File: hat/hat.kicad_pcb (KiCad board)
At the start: 4 copper layers, 45 parts, among them IC1 LM2676S-5.0, IC2 DMMT5401-7-F, J1 Conn_Coaxial, J2 nfc, J3 52840 tx pri rx, J4 52840 rx rpi tx, J5 Conn_ARM_JTAG_SWD_10, J6 Raspberry_Pi_2_3, J7 Screw_Terminal_01x02, J8 Screw_Terminal_01x01, P1 Conn_02x08_Odd_Even, P2 Conn_02x20_Odd_Even, Q1 DMG2305UX-7, U1 nRF52840-QIAA, Y1 32mhzCrystal

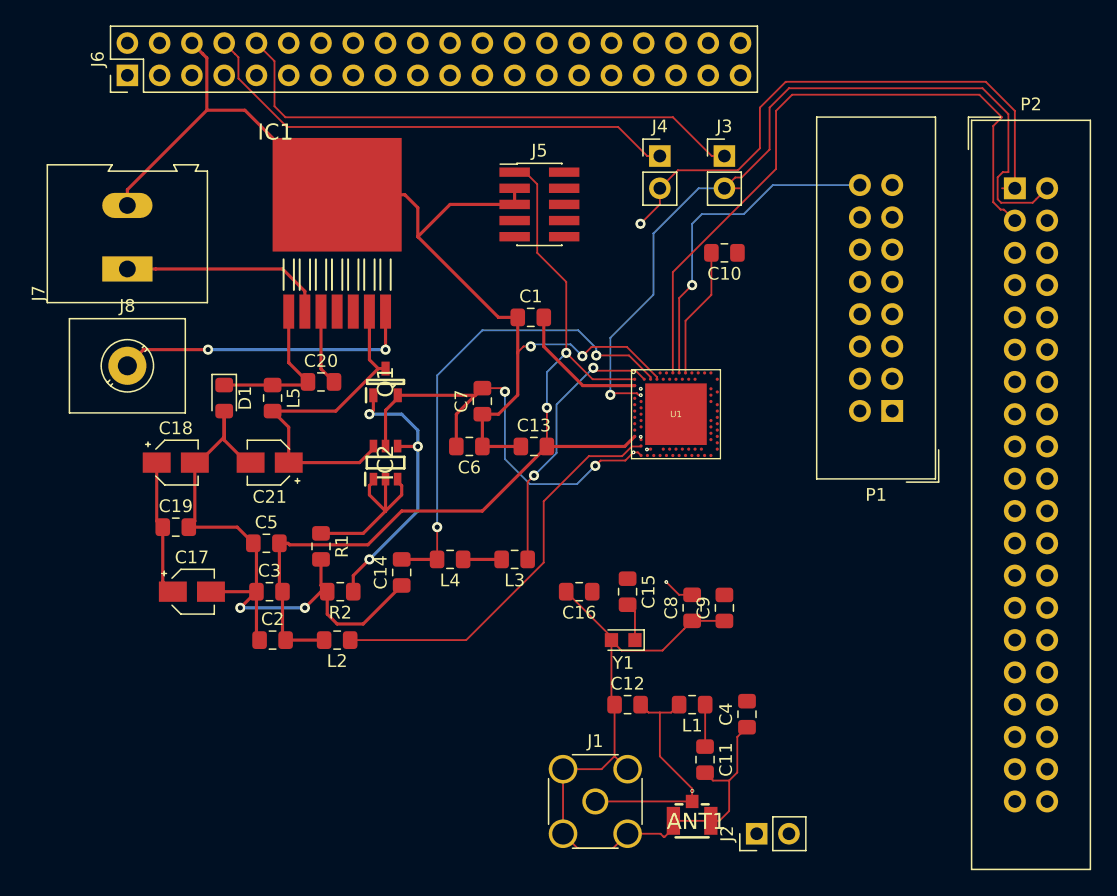
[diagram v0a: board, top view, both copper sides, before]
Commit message: made more connections please note this is completely manually routed
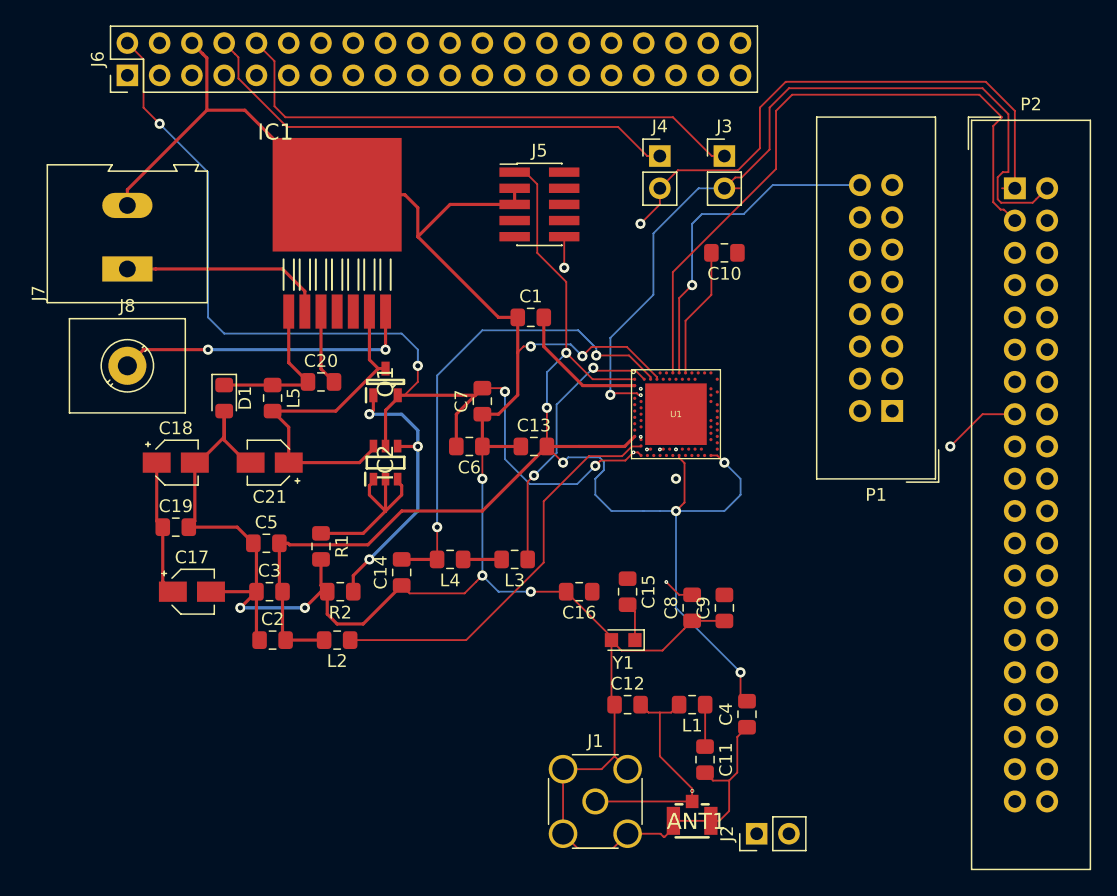
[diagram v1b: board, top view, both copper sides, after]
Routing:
- net P0.14: track 0.00 -> 48.3 mm, vias 0 -> 2
- net VDD(A14): track 73.0 -> 120.2 mm, vias 2 -> 6
- net VDDH: track 38.3 -> 84.6 mm, vias 4 -> 6
- net P0.18: track 0.00 -> 31.9 mm, vias 0 -> 3
- net Ground (VSS_PA): track 200.6 -> 225.0 mm, vias 4 -> 7
- net (no net): track 0.00 -> 3.18 mm

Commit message: added  more traces what more can i say
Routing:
- net P0.16: track 0.00 -> 40.3 mm, vias 0 -> 2
- net P0.19: track 0.00 -> 35.5 mm, vias 0 -> 2
- net SWDIO: track 0.00 -> 35.4 mm, vias 0 -> 2
- net SWDCLK: track 0.00 -> 34.4 mm, vias 0 -> 2
- net P0.21: track 0.00 -> 33.1 mm, vias 0 -> 2
- net P0.23: track 0.00 -> 31.7 mm, vias 0 -> 2
- net P0.25: track 0.00 -> 30.4 mm, vias 0 -> 2
- net XC1: track 0.00 -> 25.5 mm, vias 0 -> 3
- net ant: track 3.31 -> 27.6 mm, vias 0 -> 2
- net XC2: track 0.00 -> 22.7 mm, vias 0 -> 3
- net +12V: track 27.0 -> 44.5 mm
- net Ground (VSS_PA): track 225.0 -> 236.3 mm, vias 7 -> 10
- net VDD(A14): track 120.2 -> 127.9 mm, vias 6 -> 9
- net P0.14: track 48.3 -> 43.4 mm
- net P0.27: track 0.00 -> 2.15 mm, vias 0 -> 1
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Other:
- rule via_min_size: 0.15 -> 0.2

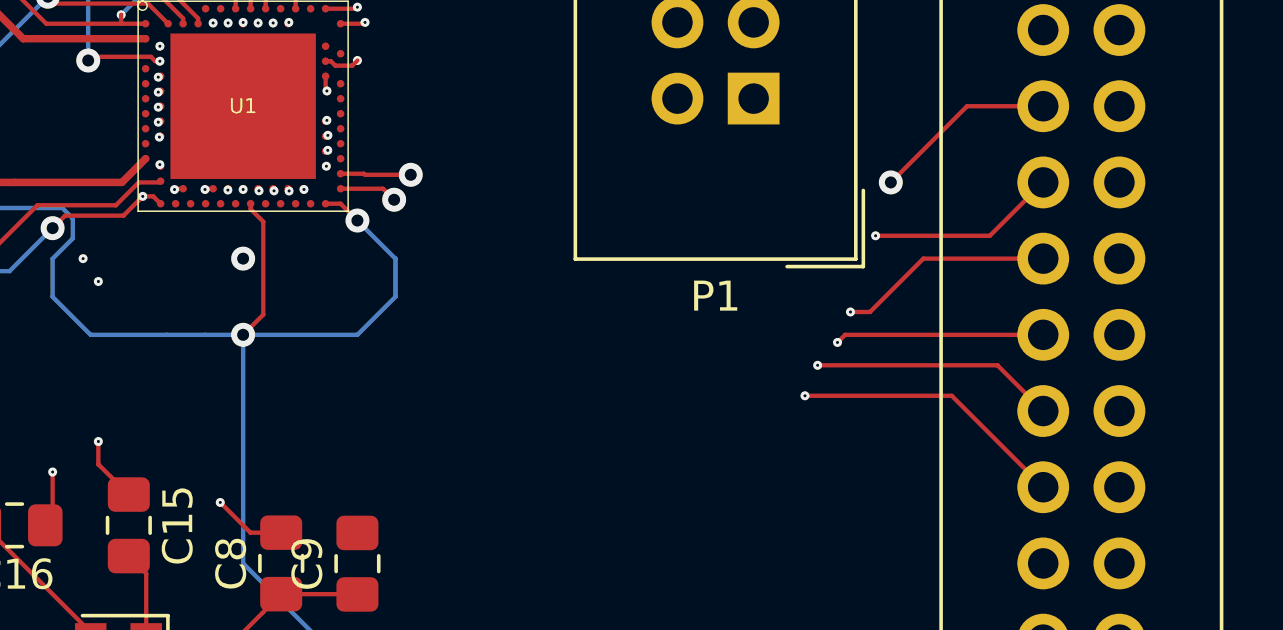
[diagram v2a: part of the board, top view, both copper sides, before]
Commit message: more traces added
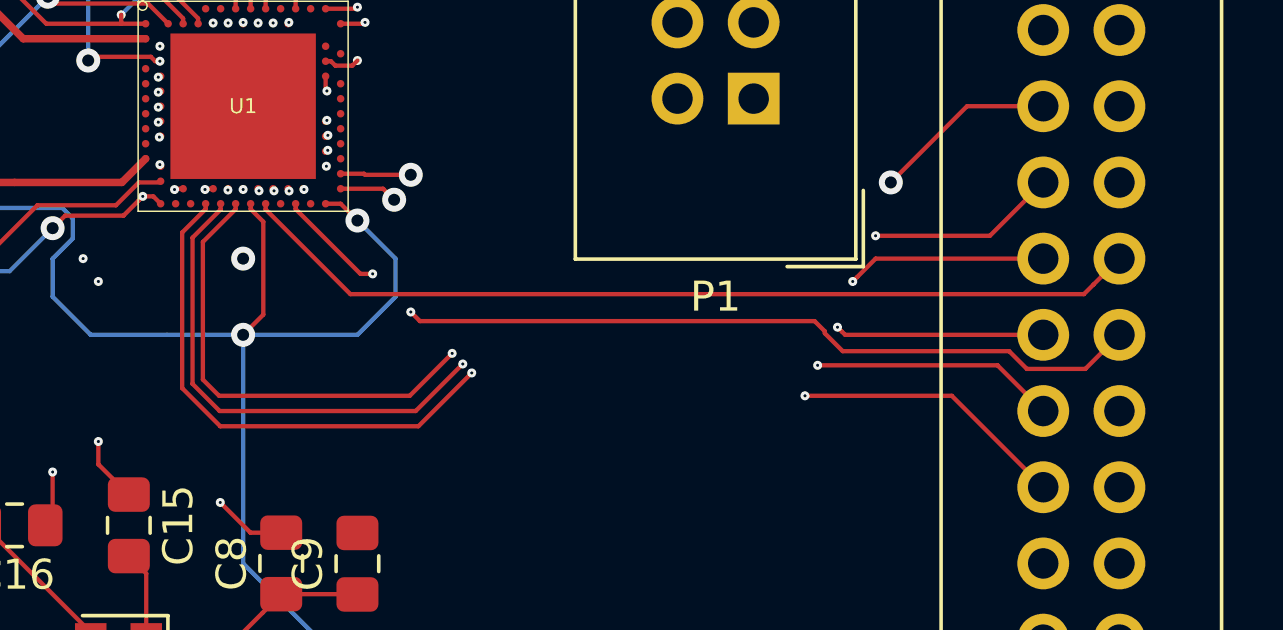
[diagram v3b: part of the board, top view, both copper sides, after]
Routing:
- net P0.24: track 0.00 -> 30.4 mm, vias 0 -> 2
- net P0.20: track 0.00 -> 30.3 mm
- net P0.13: track 0.00 -> 17.4 mm, vias 0 -> 1
- net P0.15: track 0.00 -> 16.4 mm, vias 0 -> 1
- net P0.17: track 0.00 -> 15.4 mm, vias 0 -> 1
- net P0.19: track 35.5 -> 36.0 mm
- net P0.21: track 33.1 -> 33.6 mm

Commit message: added reference files
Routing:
- net P0.05: track 1.60 -> 57.2 mm, vias 1 -> 3
- net P0.07: track 1.80 -> 56.8 mm, vias 1 -> 3
- net P0.03: track 1.31 -> 52.7 mm, vias 1 -> 2
- net P1.12: track 1.30 -> 45.0 mm, vias 1 -> 2
- net P1.14: track 1.31 -> 44.1 mm, vias 1 -> 2
- net P0.11: track 1.82 -> 43.7 mm, vias 1 -> 3
- net P0.27: track 2.15 -> 41.7 mm, vias 1 -> 3
- net P1.08: track 1.84 -> 30.9 mm, vias 1 -> 3
- net P1.10: track 0.00 -> 22.2 mm
- net P1.11: track 1.32 -> 21.4 mm, vias 1 -> 2
- net Ground (VSS_PA): track 236.3 -> 245.7 mm, vias 10 -> 12
- net XC2: track 22.7 -> 28.1 mm
- net XC1: track 25.5 -> 30.0 mm
- net SWDCLK: track 34.4 -> 31.6 mm
- net P0.01: track 65.1 -> 67.5 mm
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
